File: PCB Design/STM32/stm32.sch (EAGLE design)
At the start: 68 parts, among them IC1 NCP1117ST50T3G, Q1 ABM3B-8.000MHZ-10-1UT, T5 BC847, T6 BC847, T7 BC847, T8 BC847, U1 STM32F103RET6, U2 MCP1700T-3302E/TT, U3 MCP1700T-3302E/TT, U4 MPU-6050, U5 TB6612FNG, X1 22-23-2031

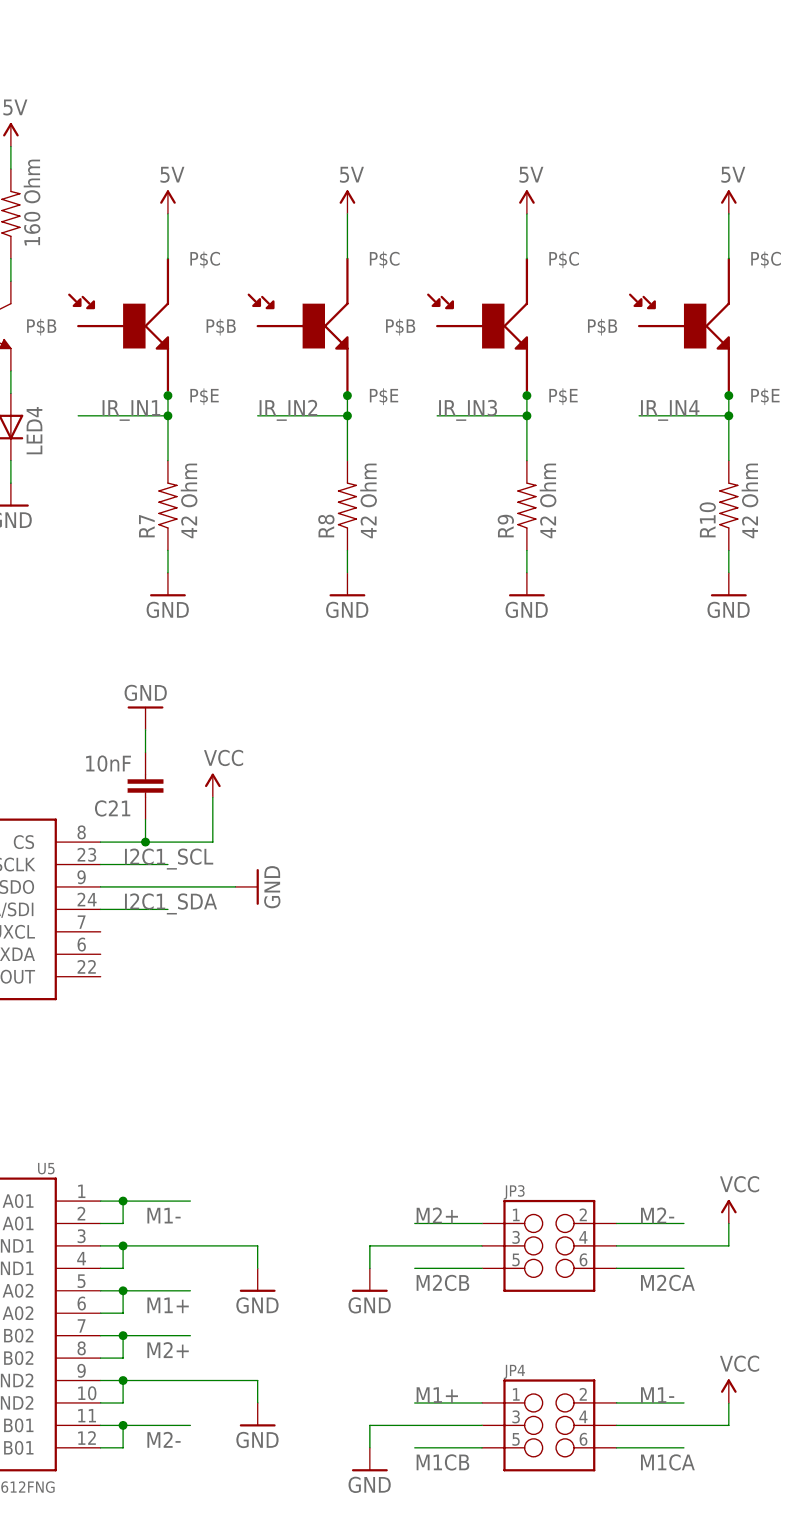
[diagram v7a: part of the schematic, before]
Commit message: updated power to phototransistors and the encoders
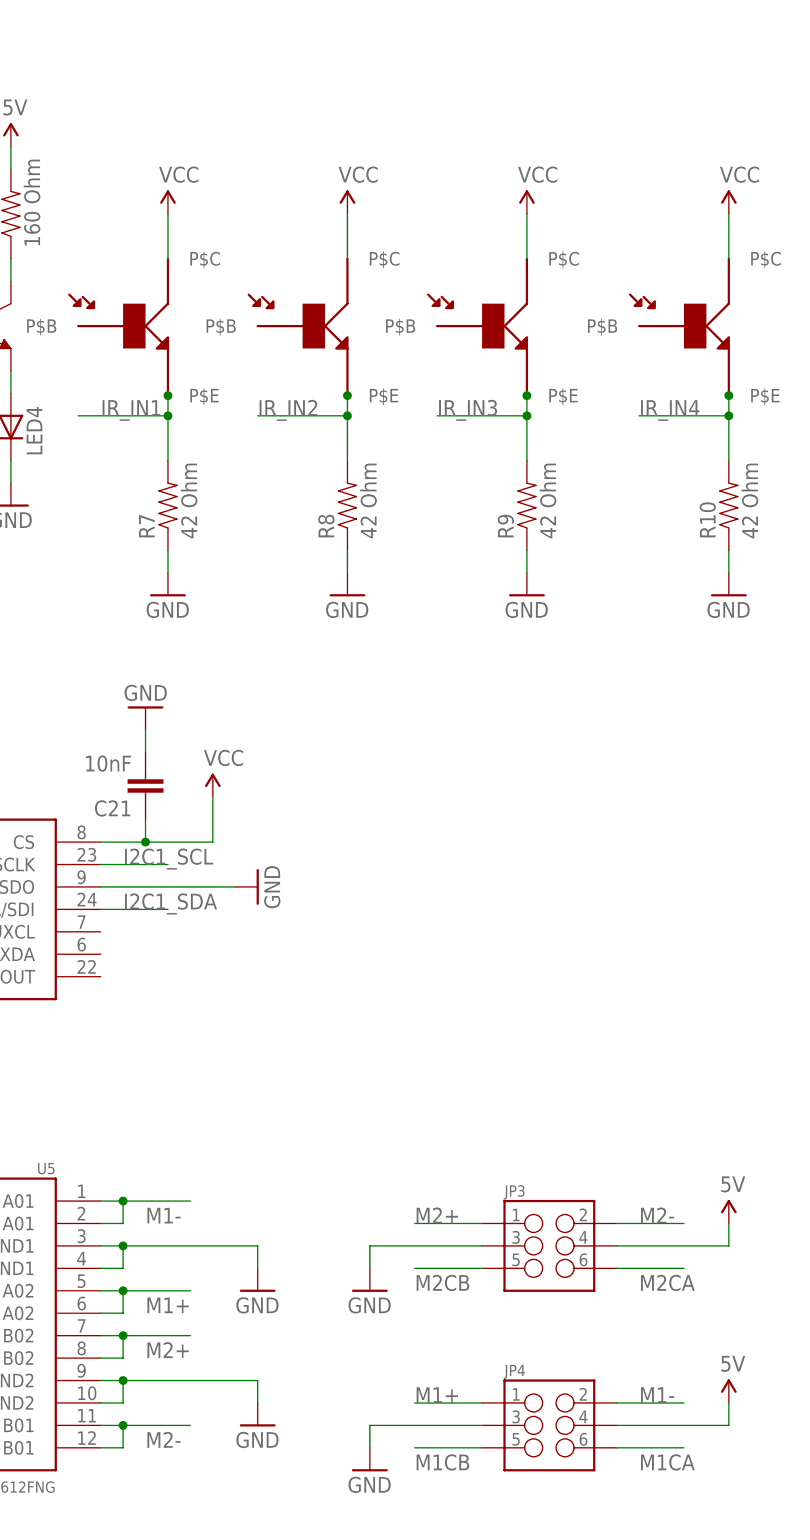
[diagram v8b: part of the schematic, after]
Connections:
- net 5V: now also JP3.4, JP4.4; no longer U$2.P$C, U$3.P$C, U$4.P$C, U$5.P$C
- net VCC: now also U$2.P$C, U$3.P$C, U$4.P$C, U$5.P$C; no longer JP3.4, JP4.4
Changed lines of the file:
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@@
 <part name="GND24" library="SparkFun-Aesthetics" deviceset="GND" device=""/>
 <part name="GND23" library="SparkFun-Aesthetics" deviceset="GND" device=""/>
-<part name="SUPPLY14" library="SparkFun-Aesthetics" deviceset="VCC" device=""/>
-<part name="SUPPLY15" library="SparkFun-Aesthetics" deviceset="VCC" device=""/>
 <part name="C17" library="SparkFun-Capacitors" deviceset="CAP" device="0805" value="0.1uF"/>
 <part name="SUPPLY3" library="SparkFun-Aesthetics" deviceset="VCC" device=""/>
@@
 <part name="SUPPLY7" library="SparkFun-Aesthetics" deviceset="5V" device=""/>
 <part name="SUPPLY8" library="SparkFun-Aesthetics" deviceset="5V" device=""/>
-<part name="SUPPLY9" library="SparkFun-Aesthetics" deviceset="5V" device=""/>
-<part name="SUPPLY10" library="SparkFun-Aesthetics" deviceset="5V" device=""/>
-<part name="SUPPLY12" library="SparkFun-Aesthetics" deviceset="5V" device=""/>
-<part name="SUPPLY13" library="SparkFun-Aesthetics" deviceset="5V" device=""/>
 <part name="GND27" library="SparkFun-Aesthetics" deviceset="GND" device=""/>
 <part name="GND28" library="SparkFun-Aesthetics" deviceset="GND" device=""/>
@@
 <part name="U$4" library="phototransistor" deviceset="PHTRST" device=""/>
 <part name="U$5" library="phototransistor" deviceset="PHTRST" device=""/>
+<part name="SUPPLY9" library="SparkFun-Aesthetics" deviceset="VCC" device=""/>
+<part name="SUPPLY10" library="SparkFun-Aesthetics" deviceset="VCC" device=""/>
+<part name="SUPPLY12" library="SparkFun-Aesthetics" deviceset="VCC" device=""/>
+<part name="SUPPLY13" library="SparkFun-Aesthetics" deviceset="VCC" device=""/>
+<part name="SUPPLY19" library="SparkFun-Aesthetics" deviceset="5V" device=""/>
+<part name="SUPPLY23" library="SparkFun-Aesthetics" deviceset="5V" device=""/>
 </parts>
 <sheets>
@@
 <instance part="GND24" gate="1" x="388.62" y="106.68"/>
 <instance part="GND23" gate="1" x="388.62" y="127"/>
-<instance part="SUPPLY14" gate="G$1" x="429.26" y="134.62"/>
-<instance part="SUPPLY15" gate="G$1" x="429.26" y="114.3"/>
 <instance part="C17" gate="G$1" x="302.26" y="121.92"/>
 <instance part="SUPPLY3" gate="G$1" x="302.26" y="132.08"/>
@@
 <instance part="SUPPLY7" gate="G$1" x="322.58" y="256.54"/>
 <instance part="SUPPLY8" gate="G$1" x="347.98" y="256.54"/>
-<instance part="SUPPLY9" gate="G$1" x="365.76" y="248.92"/>
-<instance part="SUPPLY10" gate="G$1" x="386.08" y="248.92"/>
-<instance part="SUPPLY12" gate="G$1" x="406.4" y="248.92"/>
-<instance part="SUPPLY13" gate="G$1" x="429.26" y="248.92"/>
 <instance part="GND27" gate="1" x="109.22" y="83.82"/>
 <instance part="GND28" gate="1" x="127" y="83.82"/>
@@
 <instance part="U$4" gate="G$1" x="403.86" y="236.22"/>
 <instance part="U$5" gate="G$1" x="426.72" y="236.22"/>
+<instance part="SUPPLY9" gate="G$1" x="365.76" y="248.92"/>
+<instance part="SUPPLY10" gate="G$1" x="386.08" y="248.92"/>
+<instance part="SUPPLY12" gate="G$1" x="406.4" y="248.92"/>
+<instance part="SUPPLY13" gate="G$1" x="429.26" y="248.92"/>
+<instance part="SUPPLY19" gate="G$1" x="429.26" y="134.62"/>
+<instance part="SUPPLY23" gate="G$1" x="429.26" y="114.3"/>
 </instances>
 <busses>
@@
 </segment>
 <segment>
-<pinref part="JP4" gate="G$1" pin="4"/>
-<wire x1="416.56" y1="111.76" x2="429.26" y2="111.76" width="0.1524" layer="91"/>
-<pinref part="SUPPLY15" gate="G$1" pin="VCC"/>
-<wire x1="429.26" y1="114.3" x2="429.26" y2="111.76" width="0.1524" layer="91"/>
-</segment>
-<segment>
-<pinref part="JP3" gate="G$1" pin="4"/>
-<wire x1="416.56" y1="132.08" x2="429.26" y2="132.08" width="0.1524" layer="91"/>
-<pinref part="SUPPLY14" gate="G$1" pin="VCC"/>
-<wire x1="429.26" y1="134.62" x2="429.26" y2="132.08" width="0.1524" layer="91"/>
-</segment>
-<segment>
 <pinref part="U5" gate="G$1" pin="VCC"/>
 <wire x1="325.12" y1="127" x2="312.42" y2="127" width="0.1524" layer="91"/>
@@
 <wire x1="238.76" y1="190.5" x2="238.76" y2="185.42" width="0.1524" layer="91"/>
 </segment>
+<segment>
+<wire x1="365.76" y1="248.92" x2="365.76" y2="243.84" width="0.1524" layer="91"/>
+<pinref part="U$2" gate="G$1" pin="P$C"/>
+<pinref part="SUPPLY9" gate="G$1" pin="VCC"/>
+</segment>
+<segment>
+<wire x1="386.08" y1="248.92" x2="386.08" y2="243.84" width="0.1524" layer="91"/>
+<pinref part="U$3" gate="G$1" pin="P$C"/>
+<pinref part="SUPPLY10" gate="G$1" pin="VCC"/>
+</segment>
+<segment>
+<wire x1="406.4" y1="248.92" x2="406.4" y2="243.84" width="0.1524" layer="91"/>
+<pinref part="U$4" gate="G$1" pin="P$C"/>
+<pinref part="SUPPLY12" gate="G$1" pin="VCC"/>
+</segment>
+<segment>
+<wire x1="429.26" y1="248.92" x2="429.26" y2="243.84" width="0.1524" layer="91"/>
+<pinref part="U$5" gate="G$1" pin="P$C"/>
+<pinref part="SUPPLY13" gate="G$1" pin="VCC"/>
+</segment>
 </net>
 <net name="JTAG-TRST" class="0">
@@
 <wire x1="170.18" y1="83.82" x2="170.18" y2="86.36" width="0.1524" layer="91"/>
 <pinref part="C9" gate="G$1" pin="1"/>
-</segment>
-<segment>
-<wire x1="365.76" y1="248.92" x2="365.76" y2="243.84" width="0.1524" layer="91"/>
-<pinref part="SUPPLY9" gate="G$1" pin="5V"/>
-<pinref part="U$2" gate="G$1" pin="P$C"/>
-</segment>
-<segment>
-<wire x1="386.08" y1="248.92" x2="386.08" y2="243.84" width="0.1524" layer="91"/>
-<pinref part="SUPPLY10" gate="G$1" pin="5V"/>
-<pinref part="U$3" gate="G$1" pin="P$C"/>
-</segment>
-<segment>
-<wire x1="406.4" y1="248.92" x2="406.4" y2="243.84" width="0.1524" layer="91"/>
-<pinref part="SUPPLY12" gate="G$1" pin="5V"/>
-<pinref part="U$4" gate="G$1" pin="P$C"/>
-</segment>
-<segment>
-<wire x1="429.26" y1="248.92" x2="429.26" y2="243.84" width="0.1524" layer="91"/>
-<pinref part="SUPPLY13" gate="G$1" pin="5V"/>
-<pinref part="U$5" gate="G$1" pin="P$C"/>
 </segment>
 <segment>
@@
 <wire x1="347.98" y1="254" x2="347.98" y2="256.54" width="0.1524" layer="91"/>
 </segment>
-</net>
+<segment>
+<pinref part="JP3" gate="G$1" pin="4"/>
+<wire x1="416.56" y1="132.08" x2="429.26" y2="132.08" width="0.1524" layer="91"/>
+<wire x1="429.26" y1="134.62" x2="429.26" y2="132.08" width="0.1524" layer="91"/>
+<pinref part="SUPPLY19" gate="G$1" pin="5V"/>
+</segment>
+<segment>
+<pinref part="JP4" gate="G$1" pin="4"/>
+<wire x1="416.56" y1="111.76" x2="429.26" y2="111.76" width="0.1524" layer="91"/>
+<wire x1="429.26" y1="114.3" x2="429.26" y2="111.76" width="0.1524" layer="91"/>
+<pinref part="SUPPLY23" gate="G$1" pin="5V"/>
+</segment>
+</net>
